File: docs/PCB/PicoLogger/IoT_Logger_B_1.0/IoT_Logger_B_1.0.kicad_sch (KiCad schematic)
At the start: 31 parts, among them J1 JTAG, U1 STM32F412RGTx, Y1 3225-25M-SR, Y2 32.768K-CFPX217

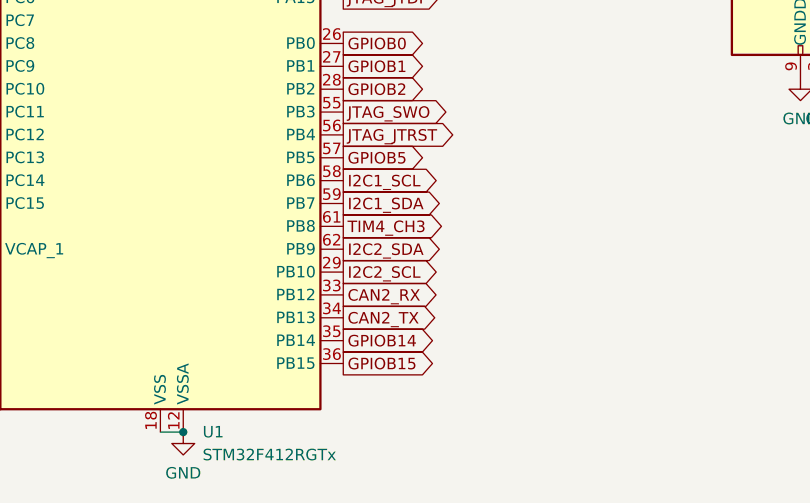
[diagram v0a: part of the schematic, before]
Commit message: Logger IoT B and C production files generated, backend and frontend prepared for new logger type.
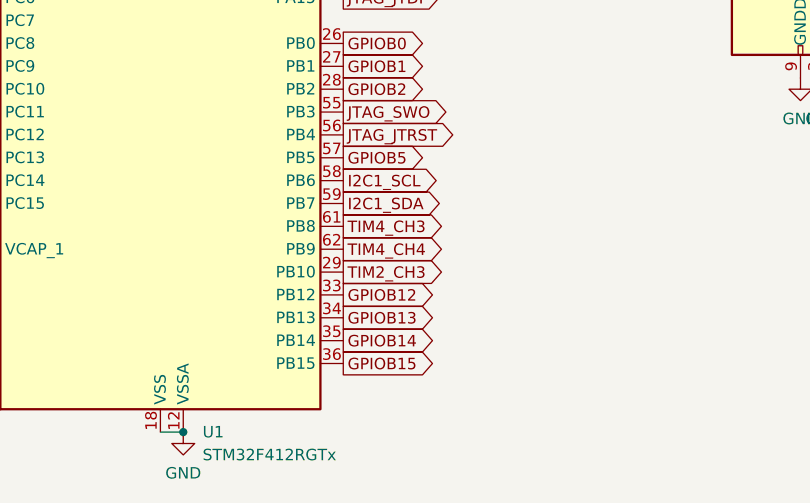
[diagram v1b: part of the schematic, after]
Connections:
- net CAN2_RX renamed GPIOB12
- net CAN2_TX renamed GPIOB13
- net I2C2_SCL renamed TIM2_CH3
- net I2C2_SDA renamed TIM4_CH4
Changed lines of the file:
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@@
+		)
+	)
+	(global_label "GPIOB12"
+		(shape output)
+		(at 171.45 146.05 0)
+		(fields_autoplaced yes)
+		(effects
+			(font
+				(size 1.27 1.27)
+			)
+			(justify left)
+		)
+		(property "Intersheetrefs" "${INTERSHEET_REFS}"
+			(at 182.5995 146.05 0)
+			(effects
+				(font
+					(size 1.27 1.27)
+				)
+				(justify left)
+				(hide yes)
+			)
 		)
 	)
@@
 		)
 	)
-	(global_label "I2C2_SCL"
+	(global_label "TIM2_CH3"
 		(shape output)
 		(at 171.45 143.51 0)
@@
 		)
 		(property "Intersheetrefs" "${INTERSHEET_REFS}"
-			(at 183.2042 143.51 0)
+			(at 183.4461 143.51 0)
 			(effects
 				(font
@@
 		)
 	)
+	(global_label "GPIOB13"
+		(shape output)
+		(at 171.45 148.59 0)
+		(fields_autoplaced yes)
+		(effects
+			(font
+				(size 1.27 1.27)
+			)
+			(justify left)
+		)
+		(property "Intersheetrefs" "${INTERSHEET_REFS}"
+			(at 182.5995 148.59 0)
+			(effects
+				(font
+					(size 1.27 1.27)
+				)
+				(justify left)
+				(hide yes)
+			)
+		)
+	)
 	(global_label "USART3_TX"
 		(shape output)
@@
 		)
 	)
-	(global_label "I2C2_SDA"
+	(global_label "TIM4_CH4"
 		(shape output)
 		(at 171.45 140.97 0)
@@
 		)
 		(property "Intersheetrefs" "${INTERSHEET_REFS}"
-			(at 183.2647 140.97 0)
+			(at 183.4461 140.97 0)
 			(effects
 				(font
@@
 		)
 	)
-	(global_label "CAN2_TX"
-		(shape output)
-		(at 171.45 148.59 0)
-		(fields_autoplaced yes)
-		(effects
-			(font
-				(size 1.27 1.27)
-			)
-			(justify left)
-		)
-		(property "Intersheetrefs" "${INTERSHEET_REFS}"
-			(at 182.4785 148.59 0)
-			(effects
-				(font
-					(size 1.27 1.27)
-				)
-				(justify left)
-				(hide yes)
-			)
-		)
-	)
 	(global_label "USART2_RX"
 		(shape output)
@@
 				(hide yes)
 			)
-		)
-	)
-	(global_label "CAN2_RX"
-		(shape output)
-		(at 171.45 146.05 0)
-		(fields_autoplaced yes)
-		(effects
-			(font
-				(size 1.27 1.27)
-			)
-			(justify left)
-		)
-		(property "Intersheetrefs" "${INTERSHEET_REFS}"
-			(at 182.7809 146.05 0)
-			(effects
-				(font
-					(size 1.27 1.27)
-				)
-				(justify left)
-				(hide yes)
-			)

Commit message: Code added, documentation review.
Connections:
- net JTAG_JTRST renamed GPIOB4
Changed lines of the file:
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@@
 		)
 	)
-	(global_label "JTAG_JTRST"
+	(global_label "GPIOB4"
 		(shape output)
 		(at 171.45 128.27 0)
@@
 		)
 		(property "Intersheetrefs" "${INTERSHEET_REFS}"
-			(at 185.0789 128.27 0)
+			(at 181.39 128.27 0)
 			(effects
 				(font
